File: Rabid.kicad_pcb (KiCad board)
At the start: 2 copper layers, 344.6 x 122 mm, 192 parts, among them J1 USB Header, SW1 Esc, SW10 A, SW102 →, SW11 Z, SW12 LMeta, SW13 F1, SW14 2, SW15 W, SW16 S, SW17 X, SW18 LAlt, SW19 F2, SW2 Tilde, SW20 3, SW21 E, SW22 D, SW23 C, SW25 F3, SW26 4, SW27 R, SW28 F, SW29 V, SW3 Tab, SW31 F4, SW32 5, SW33 T, SW34 G, SW35 B, SW37 F5, SW38 6, SW39 Y, SW4 CapsLk, SW40 H, SW41 N, SW42 Space, SW43 F6, SW44 7, SW45 U, SW46 J, SW47 M, SW49 F7, SW5 LShift, SW50 8, SW51 I, SW52 K, SW53 ,, SW55 F8, SW56 9, SW57 O, SW58 L, SW59 ., SW6 LCtrl, SW61 F9, SW62 0, SW63 P, SW64 ;, SW65 /, SW66 AltGr, SW67 F10, SW68 -, SW69 [, SW70 ", SW71 RShift, SW72 RMeta, SW73 F11, SW74 =, SW75 ], SW76 ↲, SW78 Fn, SW79 F12, SW8 1, SW80 BkSpc, SW81 \, SW84 RCtrl, SW85 PrtSc, SW86 Ins, SW87 Del, SW9 Q, SW90 ←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

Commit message: Adjusted location of keys to match plate mount holes.
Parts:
- moved SW102 0.27 mm to (378.8, 184.9)
- moved SW90 0.27 mm to (340.7, 184.9)
- moved SW96 0.27 mm to (359.8, 184.9)
- moved D102 0.25 mm to (367.0, 194.8)
- moved D105 0.25 mm to (356.0, 90.8)
- moved D106 0.25 mm to (365.5, 99.8)
- moved D108 0.25 mm to (355.8, 99.6)
- moved D85 0.25 mm to (328.7, 90.8)
- moved D86 0.25 mm to (328.7, 118.7)
- moved D87 0.25 mm to (328.7, 137.8)
- moved D90 0.25 mm to (342.1, 180.6)
- moved D91 0.25 mm to (347.7, 90.8)
- moved D92 0.25 mm to (347.7, 118.7)
- moved D93 0.25 mm to (347.7, 137.8)
- moved D96 0.25 mm to (347.7, 194.8)
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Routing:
- net Row0: track 359.7 -> 360.9 mm

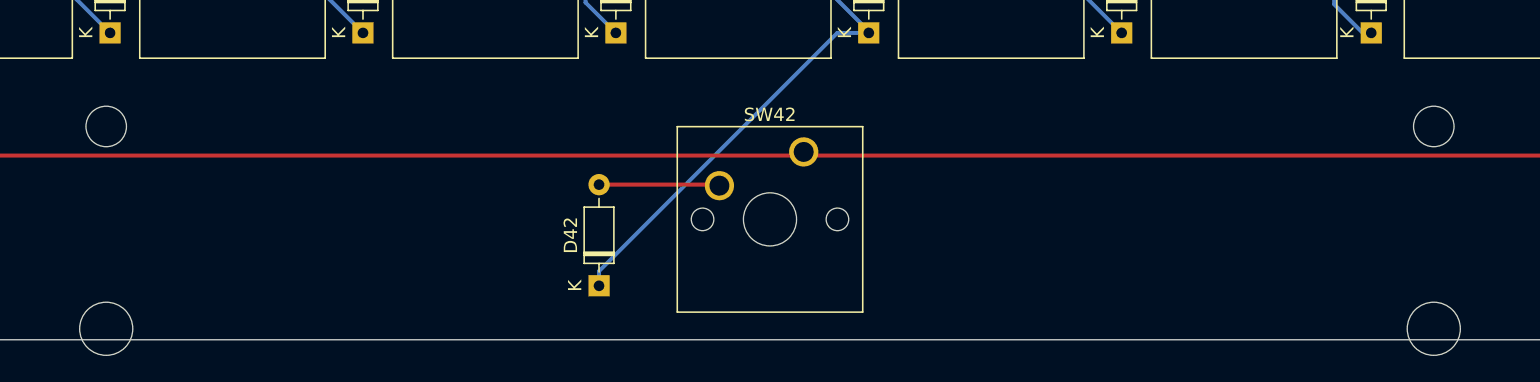
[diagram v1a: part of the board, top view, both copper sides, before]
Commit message: Flip stabilizers on spacebar to fit on the board.
Spacebar footprint is now broken out into its own library.
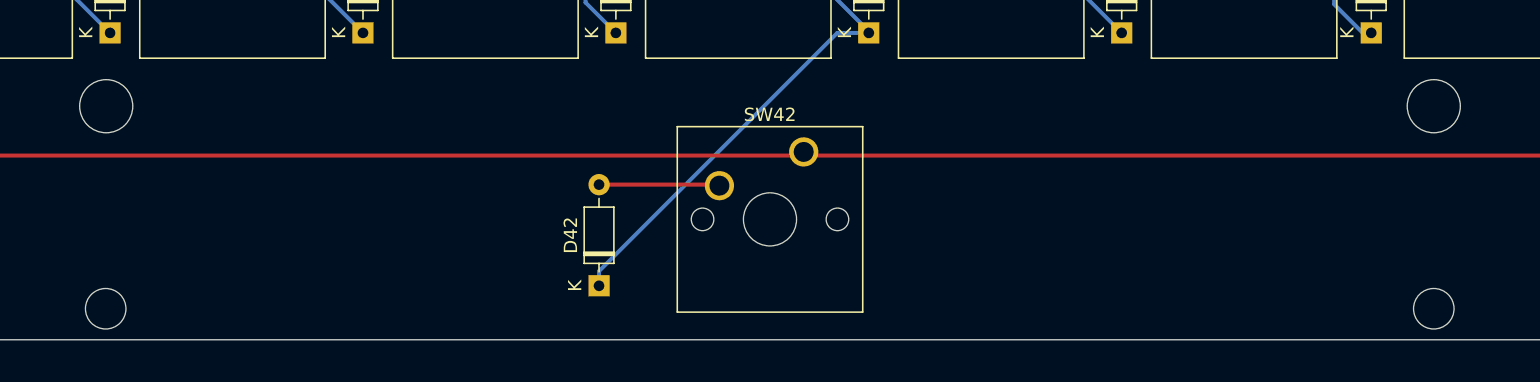
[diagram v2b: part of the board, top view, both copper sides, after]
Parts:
- SW42: footprint Button_Switch_Keyboard:SW_Cherry_MX_6.25u_PCB -> RabidKeyboard:SW_Cherry_MX_6.25u_PCB_MirroredStabs
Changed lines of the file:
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@@
     )
   )
-  (footprint "Button_Switch_Keyboard:SW_Cherry_MX_6.25u_PCB" (layer "F.Cu")
+  (footprint "RabidKeyboard:SW_Cherry_MX_6.25u_PCB_MirroredStabs" (layer "F.Cu")
     (at 171.6278 184.8612)
     (descr "Cherry MX keyswitch, 6.25u, PCB mount, http://cherryamericas.com/wp-content/uploads/2014/12/mx_cat.pdf")
@@
       (effects (font (size 1 1) (thickness 0.15)))
     )
-    (fp_line (start 4.445 12.065) (end -9.525 12.065) (layer "F.SilkS") (width 0.12))
     (fp_line (start 4.445 -1.905) (end 4.445 12.065) (layer "F.SilkS") (width 0.12))
     (fp_line (start -9.525 -1.905) (end 4.445 -1.905) (layer "F.SilkS") (width 0.12))
     (fp_line (start -9.525 12.065) (end -9.525 -1.905) (layer "F.SilkS") (width 0.12))
+    (fp_line (start 4.445 12.065) (end -9.525 12.065) (layer "F.SilkS") (width 0.12))
     (fp_line (start -62.07125 14.605) (end -62.07125 -4.445) (layer "Dwgs.User") (width 0.15))
+    (fp_line (start -62.07125 -4.445) (end 56.99125 -4.445) (layer "Dwgs.User") (width 0.15))
     (fp_line (start 56.99125 14.605) (end -62.07125 14.605) (layer "Dwgs.User") (width 0.15))
     (fp_line (start 56.99125 -4.445) (end 56.99125 14.605) (layer "Dwgs.User") (width 0.15))
-    (fp_line (start -62.07125 -4.445) (end 56.99125 -4.445) (layer "Dwgs.User") (width 0.15))
+    (fp_line (start 4.06 11.68) (end -9.14 11.68) (layer "F.CrtYd") (width 0.05))
     (fp_line (start -9.14 11.68) (end -9.14 -1.52) (layer "F.CrtYd") (width 0.05))
     (fp_line (start 4.06 -1.52) (end 4.06 11.68) (layer "F.CrtYd") (width 0.05))
     (fp_line (start -9.14 -1.52) (end 4.06 -1.52) (layer "F.CrtYd") (width 0.05))
-    (fp_line (start 4.06 11.68) (end -9.14 11.68) (layer "F.CrtYd") (width 0.05))
+    (fp_line (start -8.89 11.43) (end -8.89 -1.27) (layer "F.Fab") (width 0.1))
+    (fp_line (start 3.81 -1.27) (end 3.81 11.43) (layer "F.Fab") (width 0.1))
     (fp_line (start 3.81 11.43) (end -8.89 11.43) (layer "F.Fab") (width 0.1))
-    (fp_line (start -8.89 11.43) (end -8.89 -1.27) (layer "F.Fab") (width 0.1))
     (fp_line (start -8.89 -1.27) (end 3.81 -1.27) (layer "F.Fab") (width 0.1))
-    (fp_line (start 3.81 -1.27) (end 3.81 11.43) (layer "F.Fab") (width 0.1))
-    (pad "" np_thru_hole circle (at 47.46 13.32) (size 4 4) (drill 4) (layers *.Cu *.Mask))
-    (pad "" np_thru_hole circle (at -52.54 -1.92) (size 3.05 3.05) (drill 3.05) (layers *.Cu *.Mask))
+    (pad "" np_thru_hole circle (at -52.54 -3.445) (size 4 4) (drill 4) (layers *.Cu *.Mask))
     (pad "" np_thru_hole circle (at 2.54 5.08) (size 1.7 1.7) (drill 1.7) (layers *.Cu *.Mask))
-    (pad "" np_thru_hole circle (at 47.46 -1.92) (size 3.05 3.05) (drill 3.05) (layers *.Cu *.Mask))
     (pad "" np_thru_hole circle (at -2.54 5.08) (size 4 4) (drill 4) (layers *.Cu *.Mask))
-    (pad "" np_thru_hole circle (at -52.54 13.32) (size 4 4) (drill 4) (layers *.Cu *.Mask))
+    (pad "" np_thru_hole circle (at 47.46 -3.445) (size 4 4) (drill 4) (layers *.Cu *.Mask))
     (pad "" np_thru_hole circle (at -7.62 5.08) (size 1.7 1.7) (drill 1.7) (layers *.Cu *.Mask))
+    (pad "" np_thru_hole circle (at -52.578 11.811) (size 3.05 3.05) (drill 3.05) (layers *.Cu *.Mask))
+    (pad "" np_thru_hole circle (at 47.46 11.811) (size 3.05 3.05) (drill 3.05) (layers *.Cu *.Mask))
     (pad "1" thru_hole circle (at 0 0) (size 2.2 2.2) (drill 1.5) (layers *.Cu *.Mask)
       (net 110 "Row0") (pinfunction "1") (pintype "passive"))
@@
   )
   (gr_rect (start 39.37 76.962) (end 383.921 199.009) (layer "Edge.Cuts") (width 0.1) (fill none))
-  (dimension (type aligned) (layer "Eco2.User")
-    (pts (xy 238.125 75.565) (xy 247.65 75.565))
-    (height -1.905)
-    (gr_text "0.3750 in" (at 242.8875 72.51) (layer "Eco2.User")
+  (dimension (type aligned) (layer "Cmts.User")
+    (pts (xy 323.85 76.2) (xy 328.676 76.2))
+    (height -2.159)
+    (gr_text "0.1900 in" (at 326.263 72.891) (layer "Cmts.User")
       (effects (font (size 1 1) (thickness 0.15)))
     )
@@
     (style (thickness 0.15) (arrow_length 1.27) (text_position_mode 0) (extension_height 0.58642) (extension_offset 0.5) keep_text_aligned)
   )
-  (dimension (type aligned) (layer "Eco2.User")
-    (pts (xy 37.490399 94.615) (xy 37.490399 104.14))
-    (height 1.269999)
-    (gr_text "0.3750 in" (at 35.0704 99.3775 90) (layer "Eco2.User")
+  (dimension (type aligned) (layer "Cmts.User")
+    (pts (xy 38.1 104.1908) (xy 38.1 95.25))
+    (height -3.683)
+    (gr_text "0.3520 in" (at 33.267 99.7204 90) (layer "Cmts.User")
       (effects (font (size 1 1) (thickness 0.15)))
     )
@@
     (style (thickness 0.15) (arrow_length 1.27) (text_position_mode 0) (extension_height 0.58642) (extension_offset 0.5) keep_text_aligned)
   )
-  (dimension (type aligned) (layer "Eco2.User")
-    (pts (xy 152.4 75.565) (xy 161.925 75.565))
-    (height -1.905)
-    (gr_text "0.3750 in" (at 157.1625 72.51) (layer "Eco2.User")
+  (dimension (type aligned) (layer "Cmts.User")
+    (pts (xy 57.15 76.2) (xy 76.2 76.2))
+    (height -2.921)
+    (gr_text "0.7500 in" (at 66.675 72.129) (layer "Cmts.User")
       (effects (font (size 1 1) (thickness 0.15)))
     )
@@
     (style (thickness 0.15) (arrow_length 1.27) (text_position_mode 0) (extension_height 0.58642) (extension_offset 0.5) keep_text_aligned)
   )
-  (dimension (type aligned) (layer "Eco2.User")
-    (pts (xy 57.15 75.565) (xy 76.2 75.565))
-    (height -2.54)
-    (gr_text "0.7500 in" (at 66.675 71.875) (layer "Eco2.User")
-      (effects (font (size 1 1) (thickness 0.15)))
-    )
+  (dimension (type aligned) (layer "Cmts.User")
+    (pts (xy 152.4 76.2) (xy 161.925 76.2))
+    (height -2.032)
+    (gr_text "0.3750 in" (at 157.1625 73.018) (layer "Cmts.User")
+      (effects (font (size 1 1) (thickness 0.15)))
+    )
+    (format (units 3) (units_format 1) (precision 4))
+    (style (thickness 0.15) (arrow_length 1.27) (text_position_mode 0) (extension_height 0.58642) (extension_offset 0.5) keep_text_aligned)
+  )
+  (dimension (type aligned) (layer "Cmts.User")
+    (pts (xy 238.125 76.2) (xy 247.65 76.2))
+    (height -2.286)
+    (gr_text "0.3750 in" (at 242.8875 72.764) (layer "Cmts.User")
+      (effects (font (size 1 1) (thickness 0.15)))
+    )

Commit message: Fixed several DRC errors.
 - Moved silkscreens into component footprints to keep them from overlapping.
 -  Re-routed USB traces as a differential pair.
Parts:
- D1, D10, D102, D11, D12, D13, D14, D15, D16, D17, D18, D19, D2, D20, D21, D22, D23, D25, D26, D27, D28, D29, D3, D31, D32, D33, D34, D35, D37, D38, D39, D4, D40, D41, D42, D43, D44, D45, D46, D47, D49, D5, D50, D51, D52, D53, D55, D56, D57, D58, D59, D6, D61, D62, D63, D64, D65, D66, D67, D68, D69, D70, D71, D72, D73, D74, D75, D76, D78, D79, D8, D80, D81, D84, D85, D86, D87, D9, D90, D91, D92, D93, D95, D96, D97, D98, D99: footprint Diode_THT:D_DO-35_SOD27_P7.62mm_Horizontal -> RabidKeyboard:D_DO-35_SOD27_P7.62mm_Horizontal
- R1, R2, R3: footprint Resistor_THT:R_Axial_DIN0204_L3.6mm_D1.6mm_P7.62mm_Horizontal -> RabidKeyboard:R_Axial_DIN0204_L3.6mm_D1.6mm_P7.62mm_Horizontal
- SW1, SW10, SW102, SW11, SW13, SW14, SW15, SW16, SW17, SW19, SW2, SW20, SW21, SW22, SW23, SW25, SW26, SW27, SW28, SW29, SW31, SW32, SW33, SW34, SW35, SW37, SW38, SW39, SW40, SW41, SW43, SW44, SW45, SW46, SW47, SW49, SW50, SW51, SW52, SW53, SW55, SW56, SW57, SW58, SW59, SW61, SW62, SW63, SW64, SW65, SW67, SW68, SW69, SW70, SW73, SW74, SW75, SW79, SW8, SW85, SW86, SW87, SW9, SW90, SW91, SW92, SW93, SW95, SW96, SW97, SW98, SW99: footprint Button_Switch_Keyboard:SW_Cherry_MX_1.00u_PCB -> RabidKeyboard:SW_Cherry_MX_1.00u_PCB
- SW12, SW18, SW6, SW66, SW72, SW78, SW84: footprint Button_Switch_Keyboard:SW_Cherry_MX_1.25u_PCB -> RabidKeyboard:SW_Cherry_MX_1.25u_PCB
- SW3, SW81: footprint Button_Switch_Keyboard:SW_Cherry_MX_1.50u_PCB -> RabidKeyboard:SW_Cherry_MX_1.50u_PCB
- SW5, SW76: footprint Button_Switch_Keyboard:SW_Cherry_MX_2.25u_PCB -> RabidKeyboard:SW_Cherry_MX_2.25u_PCB
- SW71: footprint Button_Switch_Keyboard:SW_Cherry_MX_2.75u_PCB -> RabidKeyboard:SW_Cherry_MX_2.75u_PCB
- SW80: footprint Button_Switch_Keyboard:SW_Cherry_MX_2.00u_PCB -> RabidKeyboard:SW_Cherry_MX_2.00u_PCB
- moved D10 0.51 mm to (63.2, 156.0)
- moved R1 0.25 mm to (354.3, 150.9)
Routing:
- net /USB_D+: track 75.9 -> 77.7 mm
- net /USB_D-: track 75.0 -> 76.3 mm
- net ColC: track 366.4 -> 367.6 mm
- net +5V: track 72.0 -> 72.9 mm
- net ColD: track 326.4 -> 327.0 mm
- net Net-(D10-Pad2): track 16.9 -> 16.4 mm

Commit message: Create a separate footprint for MX switches with LED.
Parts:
- removed D103: CapsKeyLED, LED_THT:LED_D3.0mm
- removed D105: ScrollKeyLED, LED_THT:LED_D3.0mm
- removed D107: FnKeyLED, LED_THT:LED_D3.0mm
- H1, H2, H3, H4, H5, H7: footprint MountingHole:MountingHole_4.3mm_M4 -> RabidKeyboard:MountingHole_.35in
- H6: footprint MountingHole:MountingHole_4.3mm_M4 -> RabidKeyboard:MountingHole_.25in
- SW4: footprint Button_Switch_Keyboard:SW_Cherry_MX_1.75u_PCB -> RabidKeyboard:SW_Cherry_MX_1.75u_PCB_LED
- SW61, SW91: footprint RabidKeyboard:SW_Cherry_MX_1.00u_PCB -> RabidKeyboard:SW_Cherry_MX_1.00u_PCB_LED
- moved D10 0.25 mm to (63.0, 156.0)
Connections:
- D104 pad 2: Net-(D103-Pad2) -> /CapsLED
- D106 pad 2: Net-(D105-Pad2) -> /ScrollLED
- D108 pad 2: Net-(D107-Pad2) -> /FnLED
- R1 pad 2: Net-(D105-Pad2) -> /ScrollLED
- R2 pad 2: Net-(D107-Pad2) -> /FnLED
- R3 pad 2: Net-(D103-Pad2) -> /CapsLED
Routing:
- net /CapsLED: track 0.00 -> 441.1 mm
- net Net-(D103-Pad2): track 440.6 -> 0.00 mm
- net Net-(D107-Pad2): track 156.6 -> 0.00 mm
- net /FnLED: track 0.00 -> 156.6 mm
- net /ScrollLED: track 0.00 -> 67.4 mm
- net Net-(D105-Pad2): track 66.9 -> 0.00 mm
- net GND: track 611.9 -> 610.2 mm
- net ColD: track 327.0 -> 328.6 mm
- net Net-(D10-Pad2): track 16.4 -> 17.1 mm

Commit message: Changed dimensions, moved function row up, added mounting hole.
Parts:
- added H8: MountingHole4mm, MountingHole:MountingHole_4mm, F.Cu at (357.3, 123.2)
- moved D13 0.13 mm to (76.2, 90.7)
- moved D19 0.13 mm to (94.6, 90.7)
- moved D25 0.13 mm to (114.3, 90.7)
- moved D31 0.13 mm to (133.3, 90.7)
- moved D37 0.13 mm to (161.3, 90.7)
- moved D43 0.13 mm to (181.0, 90.7)
- moved D49 0.13 mm to (200.0, 90.7)
- moved D55 0.13 mm to (219.1, 90.7)
- moved D61 0.13 mm to (247.7, 90.7)
- moved D67 0.13 mm to (266.7, 90.7)
- moved D73 0.13 mm to (285.8, 90.7)
- moved D79 0.13 mm to (304.8, 90.7)
- moved D85 0.13 mm to (328.7, 90.7)
- moved D91 0.13 mm to (347.7, 90.7)
- moved D97 0.13 mm to (366.8, 90.7)
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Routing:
- net ColQ: track 189.0 -> 187.9 mm
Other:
- board size 344.6 x 122 mm -> 343.4 x 121.9 mm

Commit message: Add GPIO/Debug header, bootsel, and reset switch.
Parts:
- added J3: GPIO Debug Header, Connector_PinHeader_2.54mm:PinHeader_1x09_P2.54mm_Horizontal, F.Cu at (373.1, 151.6)
- added SW103: BootSel Switch, Button_Switch_THT:SW_PUSH_6mm, B.Cu at (251.2, 96.8)
- added SW104: Reset Switch, Button_Switch_THT:SW_PUSH_6mm, B.Cu at (264.2, 96.8)
- J1: value USB Header -> USB Connector; footprint Connector_JST:JST_PH_S5B-PH-SM4-TB_1x05-1MP_P2.00mm_Horizontal -> Connector_JST:JST_PH_S5B-PH-K_1x05_P2.00mm_Horizontal
- moved J1 13.3 mm to (307.2, 103.1)
- moved D106 1.99 mm to (366.8, 98.3), turned to -90 degrees
- moved D104 1.80 mm to (347.7, 98.3), turned to -90 degrees
- moved D108 1.80 mm to (357.1, 98.3), turned to -90 degrees
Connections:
- net Net-(R1-Pad1) renamed /ScrollLED_GPIO
- net Net-(R2-Pad1) renamed /FnLED_GPIO
- net Net-(R3-Pad1) renamed /CapsLED_GPIO
- U1 pad 18: unconnected-(U1-Pad18) -> /GPIO17
- U1 pad 19: unconnected-(U1-Pad19) -> /GPIO18
- U1 pad 20: unconnected-(U1-Pad20) -> /GPIO19
- U1 pad 21: unconnected-(U1-Pad21) -> /GPIO20
- U1 pad 34: unconnected-(U1-Pad34) -> +3V3
- U1 pad 37: unconnected-(U1-Pad37) -> /SWDIO
- U1 pad 38: unconnected-(U1-Pad38) -> /SWCLK
- U1 pad 39: unconnected-(U1-Pad39) -> /~{RESET}
- U1 pad 40: unconnected-(U1-Pad40) -> /BOOTSEL
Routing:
- net /~{RESET}: track 0.00 -> 109.5 mm, vias 0 -> 2
- net GND: track 610.2 -> 513.5 mm
- net /BOOTSEL: track 0.00 -> 92.9 mm, vias 0 -> 2
- net /SWCLK: track 0.00 -> 72.5 mm
- net /SWDIO: track 0.00 -> 64.3 mm
- net +3V3: track 0.00 -> 54.0 mm
- net +5V: track 72.9 -> 114.6 mm
- net /GPIO17: track 0.00 -> 40.9 mm
- net /GPIO18: track 0.00 -> 39.4 mm
- net /GPIO20: track 0.00 -> 37.4 mm
- net /GPIO19: track 0.00 -> 36.9 mm
- net /CapsLED: track 441.1 -> 405.3 mm, vias 0 -> 1
- net /FnLED: track 156.6 -> 181.4 mm
- net ColL: track 194.0 -> 202.3 mm
- net /USB_D+: track 77.7 -> 74.5 mm
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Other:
- board text added: "+3V3"
- board text added: "+5V"
- board text added: "GND"
- board text added: "GP17"
- board text added: "GP18"
- board text added: "GP19"
- board text added: "GP20"
- board text added: "SWDCLK"
- board text added: "SWDIO"

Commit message: Add silkscreen labels and tidy microcontroller traces.
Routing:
- net ColI: track 221.7 -> 219.1 mm
- net ColH: track 241.5 -> 238.9 mm
- net Row1: track 299.9 -> 298.3 mm
- net /GPIO19: track 36.9 -> 38.3 mm
- net /GPIO20: track 37.4 -> 36.3 mm
- net ColE: track 305.4 -> 304.4 mm
- net ColA: track 413.2 -> 412.4 mm
- net ColL: track 202.3 -> 203.0 mm
- net ColJ: track 188.0 -> 187.3 mm
- net ColG: track 285.8 -> 285.1 mm
- net ColN: track 170.1 -> 169.5 mm
- net GND: track 513.5 -> 512.9 mm
- net ColQ: track 186.9 -> 187.5 mm
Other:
- board text added: "USB D+"
- board text added: "USB D-"
